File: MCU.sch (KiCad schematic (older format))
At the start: 25 parts, among them J5 ARM_JTAG_SWD_10, U4 STM32F407VGTx

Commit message: Lots of work on routing and pcb layout
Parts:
- C36, C45: footprint Capacitor_SMD:C_0603_1608Metric -> Capacitor_SMD:C_0805_2012Metric
- C50: footprint (none) -> Capacitor_SMD:C_0603_1608Metric
- D1, D2, D7: footprint (none) -> Diode_SMD:D_0603_1608Metric
- J5: footprint (none) -> KTHFS:Atmel_ICP_connector
- R14, R15, R16: footprint (none) -> Resistor_SMD:R_0603_1608Metric
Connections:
- net +3V3: now also U4.19 (VDD)
- net LED_1: now also U4.46 (PE15); no longer U4.35 (PB0)
- net LED_2: now also U4.47 (PB10); no longer U4.36 (PB1)
- net LED_3: now also U4.45 (PE14); no longer U4.37 (PB2)
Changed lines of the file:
@@
 F 0 "C36" H 8565 2546 50  0000 L CNN
 F 1 "1u" H 8565 2455 50  0000 L CNN
-F 2 "Capacitor_SMD:C_0603_1608Metric" H 8488 2350 50  0001 C CNN
+F 2 "Capacitor_SMD:C_0805_2012Metric" H 8488 2350 50  0001 C CNN
 F 3 "~" H 8450 2500 50  0001 C CNN
 	1    8450 2500
@@
 F 0 "J5" H 9150 6200 50  0000 R CNN
 F 1 "ARM_JTAG_SWD_10" H 9450 6100 50  0000 R CNN
-F 2 "" H 9100 5050 50  0001 C CNN
+F 2 "KTHFS:Atmel_ICP_connector" H 9100 5050 50  0001 C CNN
 F 3 "" H 9100 5050 50  0001 C CNN
 	1    9100 5050
@@
 F 0 "D1" H 7493 3795 50  0000 C CNN
 F 1 "LED" H 7493 3886 50  0000 C CNN
-F 2 "" H 7500 4050 50  0001 C CNN
+F 2 "Diode_SMD:D_0603_1608Metric" H 7500 4050 50  0001 C CNN
 F 3 "~" H 7500 4050 50  0001 C CNN
 	1    7500 4050
@@
 F 0 "D2" H 7493 4495 50  0000 C CNN
 F 1 "LED" H 7493 4586 50  0000 C CNN
-F 2 "" H 7500 4750 50  0001 C CNN
+F 2 "Diode_SMD:D_0603_1608Metric" H 7500 4750 50  0001 C CNN
 F 3 "~" H 7500 4750 50  0001 C CNN
 	1    7500 4750
@@
 F 0 "D7" H 7493 5195 50  0000 C CNN
 F 1 "LED" H 7493 5286 50  0000 C CNN
-F 2 "" H 7500 5450 50  0001 C CNN
+F 2 "Diode_SMD:D_0603_1608Metric" H 7500 5450 50  0001 C CNN
 F 3 "~" H 7500 5450 50  0001 C CNN
 	1    7500 5450
@@
 Wire Wire Line
 	4150 4550 4550 4550
-Text Label 5300 3650 2    59   ~ 0
+Text Label 1200 5150 0    59   ~ 0
 LED_1
-Text Label 5300 3750 2    59   ~ 0
+Text Label 5300 4650 2    59   ~ 0
 LED_2
-Text Label 5300 3850 2    59   ~ 0
+Text Label 1200 5050 0    59   ~ 0
 LED_3
 Wire Wire Line
-	4150 3650 5300 3650
-Wire Wire Line
-	4150 3750 5300 3750
-Wire Wire Line
-	4150 3850 5300 3850
+	2350 5150 1200 5150
+Wire Wire Line
+	4150 4650 5300 4650
+Wire Wire Line
+	2350 5050 1200 5050
 Text HLabel 4550 2150 2    59   Output ~ 0
 ~CS_1
@@
 F 0 "C45" H 9515 2521 50  0000 L CNN
 F 1 "1u" H 9515 2430 50  0000 L CNN
-F 2 "Capacitor_SMD:C_0603_1608Metric" H 9438 2325 50  0001 C CNN
+F 2 "Capacitor_SMD:C_0805_2012Metric" H 9438 2325 50  0001 C CNN
 F 3 "~" H 9400 2475 50  0001 C CNN
 	1    9400 2475
@@
 Connection ~ 3250 1450
 Wire Wire Line
-	3250 1450 3050 1450
+	3250 1450 3150 1450
 Connection ~ 3350 1450
 Wire Wire Line
@@
 F 0 "R14" H 1720 1896 50  0000 L CNN
 F 1 "R" H 1720 1805 50  0000 L CNN
-F 2 "" V 1580 1850 50  0001 C CNN
+F 2 "Resistor_SMD:R_0603_1608Metric" V 1580 1850 50  0001 C CNN
 F 3 "~" H 1650 1850 50  0001 C CNN
 	1    1650 1850
@@
 F 0 "R15" H 1720 2496 50  0000 L CNN
 F 1 "R" H 1720 2405 50  0000 L CNN
-F 2 "" V 1580 2450 50  0001 C CNN
+F 2 "Resistor_SMD:R_0603_1608Metric" V 1580 2450 50  0001 C CNN
 F 3 "~" H 1650 2450 50  0001 C CNN
 	1    1650 2450
@@
 F 0 "R16" H 10570 4496 50  0000 L CNN
 F 1 "10k" H 10570 4405 50  0000 L CNN
-F 2 "" V 10430 4450 50  0001 C CNN
+F 2 "Resistor_SMD:R_0603_1608Metric" V 10430 4450 50  0001 C CNN
 F 3 "~" H 10500 4450 50  0001 C CNN
 	1    10500 4450
@@
 F 0 "C50" H 10615 4996 50  0000 L CNN
 F 1 "C" H 10615 4905 50  0000 L CNN
-F 2 "" H 10538 4800 50  0001 C CNN
+F 2 "Capacitor_SMD:C_0603_1608Metric" H 10538 4800 50  0001 C CNN
 F 3 "~" H 10500 4950 50  0001 C CNN
 	1    10500 4950
@@
 Wire Notes Line
 	11050 700  7750 700
+Wire Wire Line
+	3150 1450 3150 1650
+Connection ~ 3150 1450
+Wire Wire Line
+	3150 1450 3050 1450
 $EndSCHEMATC

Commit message: More routing changes
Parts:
- added R19, R20: 0, Resistor_SMD:R_0603_1608Metric, symbol Device:R
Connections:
- net HGM: now also U4.3 (PE4); no longer U4.90 (PB4)
- net LNA_EN: now also U4.4 (PE5); no longer U4.91 (PB5)
- net MISO: now also U4.79 (PC11); no longer U4.31 (PA6)
- net MOSI: now also U4.80 (PC12); no longer U4.32 (PA7)
- net PA_EN: now also U4.5 (PE6); no longer U4.92 (PB6)
- net RF_GPIO0: now also U4.89 (PB3); no longer U4.96 (PB9)
- net RF_GPIO2: now also U4.90 (PB4); no longer U4.95 (PB8)
- net RF_GPIO3: now also U4.91 (PB5); no longer U4.93 (PB7)
- net SLCK: now also U4.78 (PC10); no longer U4.30 (PA5)
- net ~CS_1: now also R20.1; no longer U4.25 (PA2)
- net RF2_DIO5: now reaches U4.33 (PC4)
- net RF2_DIO3: now reaches U4.34 (PC5)
- net RF2_DIO4: now reaches U4.35 (PB0)
- net RF2_DIO0: now reaches U4.36 (PB1)
- net RF2_DIO1: now reaches U4.37 (PB2)
- net RF2_DIO2: now reaches U4.38 (PE7)
- net at U4.87 (PD6): now also R20.2
- new net: R19.2, U4.93 (PB7)
- new net MISO_RF2: U4.31 (PA6)
- new net MOSI_RF2: U4.32 (PA7)
- new net SLCK_RF2: U4.30 (PA5)
- new net ~RESET: R19.1
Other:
- note added: "SPI3"
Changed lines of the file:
@@
 $EndDescr
 Text HLabel 4550 2450 2    59   Output ~ 0
-SLCK
+SLCK_RF2
 Text HLabel 4550 2650 2    59   Output ~ 0
-MOSI
-Text HLabel 4550 2250 2    59   Output ~ 0
-~CS_2
+MOSI_RF2
 Text HLabel 4550 3150 2    50   Input ~ 0
 CAN_TX_1
@@
 Wire Notes Line
 	8050 6150 8050 3550
-Text HLabel 4550 4050 2    59   Output ~ 0
+Text HLabel 1950 4050 0    59   Output ~ 0
 HGM
-Text HLabel 4550 4150 2    59   Output ~ 0
+Text HLabel 1950 4150 0    59   Output ~ 0
 LNA_EN
-Text HLabel 4550 4250 2    59   Output ~ 0
+Text HLabel 1950 4250 0    59   Output ~ 0
 PA_EN
-Text HLabel 4550 4550 2    59   BiDi ~ 0
-RF_GPIO0
-Text HLabel 4550 4450 2    59   BiDi ~ 0
-RF_GPIO2
-Text HLabel 4550 4350 2    59   BiDi ~ 0
+Text HLabel 4550 4150 2    59   BiDi ~ 0
 RF_GPIO3
-Wire Wire Line
-	4550 2250 4150 2250
 Wire Wire Line
 	4150 2450 4550 2450
@@
 Text Notes 5050 5000 0    59   ~ 0
 CAN3\n\n
-Text Notes 4875 2575 0    59   ~ 0
+Text Notes 5200 2600 0    59   ~ 0
 SPI1
 Wire Wire Line
-	4150 4050 4550 4050
+	2350 4250 1950 4250
+Wire Wire Line
+	2350 4150 1950 4150
+Wire Wire Line
+	2350 4050 1950 4050
 Wire Wire Line
 	4150 4150 4550 4150
-Wire Wire Line
-	4150 4250 4550 4250
-Wire Wire Line
-	4150 4350 4550 4350
-Wire Wire Line
-	4150 4450 4550 4450
-Wire Wire Line
-	4150 4550 4550 4550
 Text Label 1200 5150 0    59   ~ 0
 LED_1
@@
 Wire Wire Line
 	2350 5050 1200 5050
-Text HLabel 4550 2150 2    59   Output ~ 0
+Text HLabel 1950 5950 0    59   Output ~ 0
 ~CS_1
-Wire Wire Line
-	4550 2150 4150 2150
 Text Notes 9100 1975 0    59   ~ 0
 VREF\n
@@
 	4150 2550 4550 2550
 Text HLabel 4550 2550 2    59   Input ~ 0
-MISO
+MISO_RF2
 Text Label 5300 3350 2    59   ~ 0
 SWCLK
@@
 Wire Wire Line
 	3150 1450 3050 1450
+Text HLabel 4550 3750 2    59   BiDi ~ 0
+RF2_DIO0
+Text HLabel 4550 3850 2    59   BiDi ~ 0
+RF2_DIO1
+Text HLabel 1950 4350 0    59   BiDi ~ 0
+RF2_DIO2
+Text HLabel 4550 5850 2    59   BiDi ~ 0
+RF2_DIO3
+Text HLabel 4550 3650 2    59   BiDi ~ 0
+RF2_DIO4
+Text HLabel 4550 5750 2    59   BiDi ~ 0
+RF2_DIO5
+Wire Wire Line
+	4550 2250 4150 2250
+Text HLabel 4550 2250 2    59   Output ~ 0
+~CS_2
+Wire Wire Line
+	5100 3450 5500 3450
+Text HLabel 5500 3450 2    59   Output ~ 0
+RESET_RF2
+Text HLabel 4550 4350 2    50   Output ~ 0
+~RESET
+$Comp
+L Device:R R19
+U 1 1 6039C6F6
+P 4300 4350
+F 0 "R19" V 4200 4300 50  0000 C CNN
+F 1 "0" V 4200 4425 50  0000 C CNN
+F 2 "Resistor_SMD:R_0603_1608Metric" V 4230 4350 50  0001 C CNN
+F 3 "~" H 4300 4350 50  0001 C CNN
+	1    4300 4350
+	0    1    1    0
+$EndComp
+Wire Wire Line
+	4450 4350 4550 4350
+Wire Wire Line
+	4550 3750 4150 3750
+Wire Wire Line
+	4550 3850 4150 3850
+Wire Wire Line
+	1950 4350 2350 4350
+Wire Wire Line
+	4550 3650 4150 3650
+Wire Wire Line
+	4550 5750 4150 5750
+Wire Wire Line
+	4550 5850 4150 5850
+$Comp
+L Device:R R20
+U 1 1 603E4876
+P 2200 5950
+F 0 "R20" V 2100 5900 50  0000 C CNN
+F 1 "0" V 2100 6025 50  0000 C CNN
+F 2 "Resistor_SMD:R_0603_1608Metric" V 2130 5950 50  0001 C CNN
+F 3 "~" H 2200 5950 50  0001 C CNN
+	1    2200 5950
+	0    -1   -1   0
+$EndComp
+Wire Wire Line
+	2050 5950 1950 5950
+Text HLabel 4550 6350 2    59   Output ~ 0
+SLCK
+Text HLabel 4550 6550 2    59   Output ~ 0
+MOSI
+Text HLabel 4550 6450 2    59   Input ~ 0
+MISO
+Wire Wire Line
+	4150 6350 4550 6350
+Wire Wire Line
+	4550 6450 4150 6450
+Text Notes 4900 6500 0    59   ~ 0
+SPI3
+Wire Wire Line
+	4550 6550 4150 6550
+Wire Wire Line
+	4150 4050 4550 4050
+Text HLabel 4550 4050 2    59   BiDi ~ 0
+RF_GPIO2
+Wire Wire Line
+	4150 3950 4550 3950
+Text HLabel 4550 3950 2    59   BiDi ~ 0
+RF_GPIO0
 $EndSCHEMATC

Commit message: Added edge cuts and silk screen comments
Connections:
- net RESET_RF2: now also U4.8 (PC14)
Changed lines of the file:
@@
 ~CS_2
 Wire Wire Line
-	5100 3450 5500 3450
-Text HLabel 5500 3450 2    59   Output ~ 0
+	4150 6750 4550 6750
+Text HLabel 4550 6750 2    59   Output ~ 0
 RESET_RF2
 Text HLabel 4550 4350 2    50   Output ~ 0

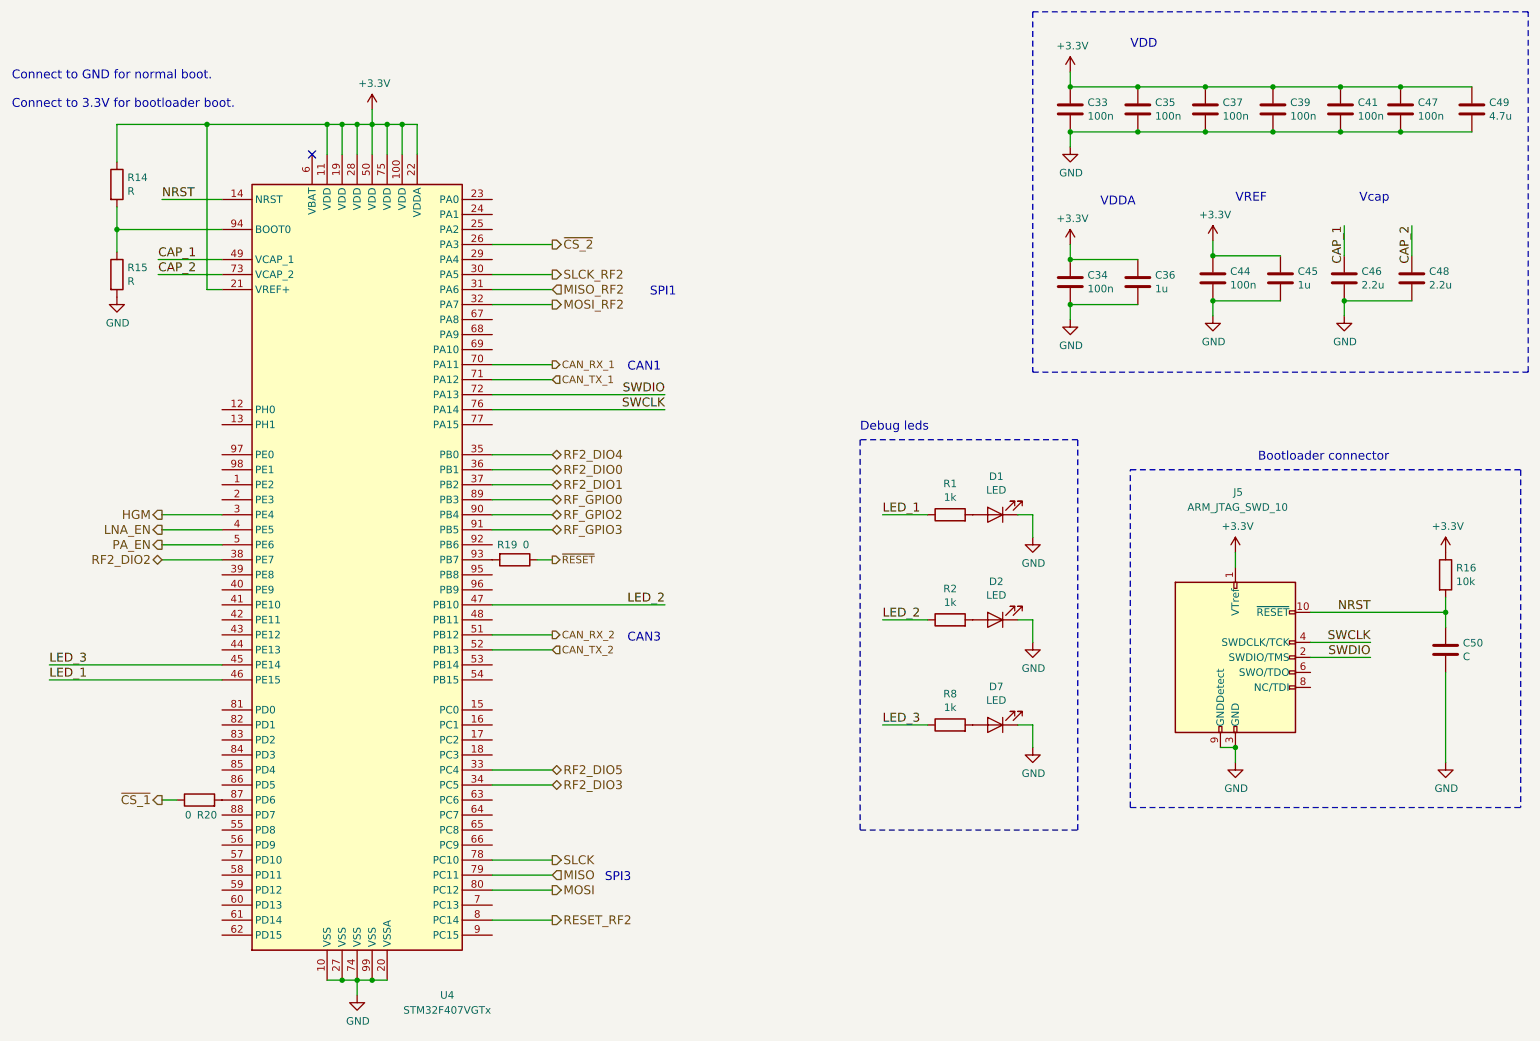
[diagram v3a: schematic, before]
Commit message: Added mounting holes and terminal block
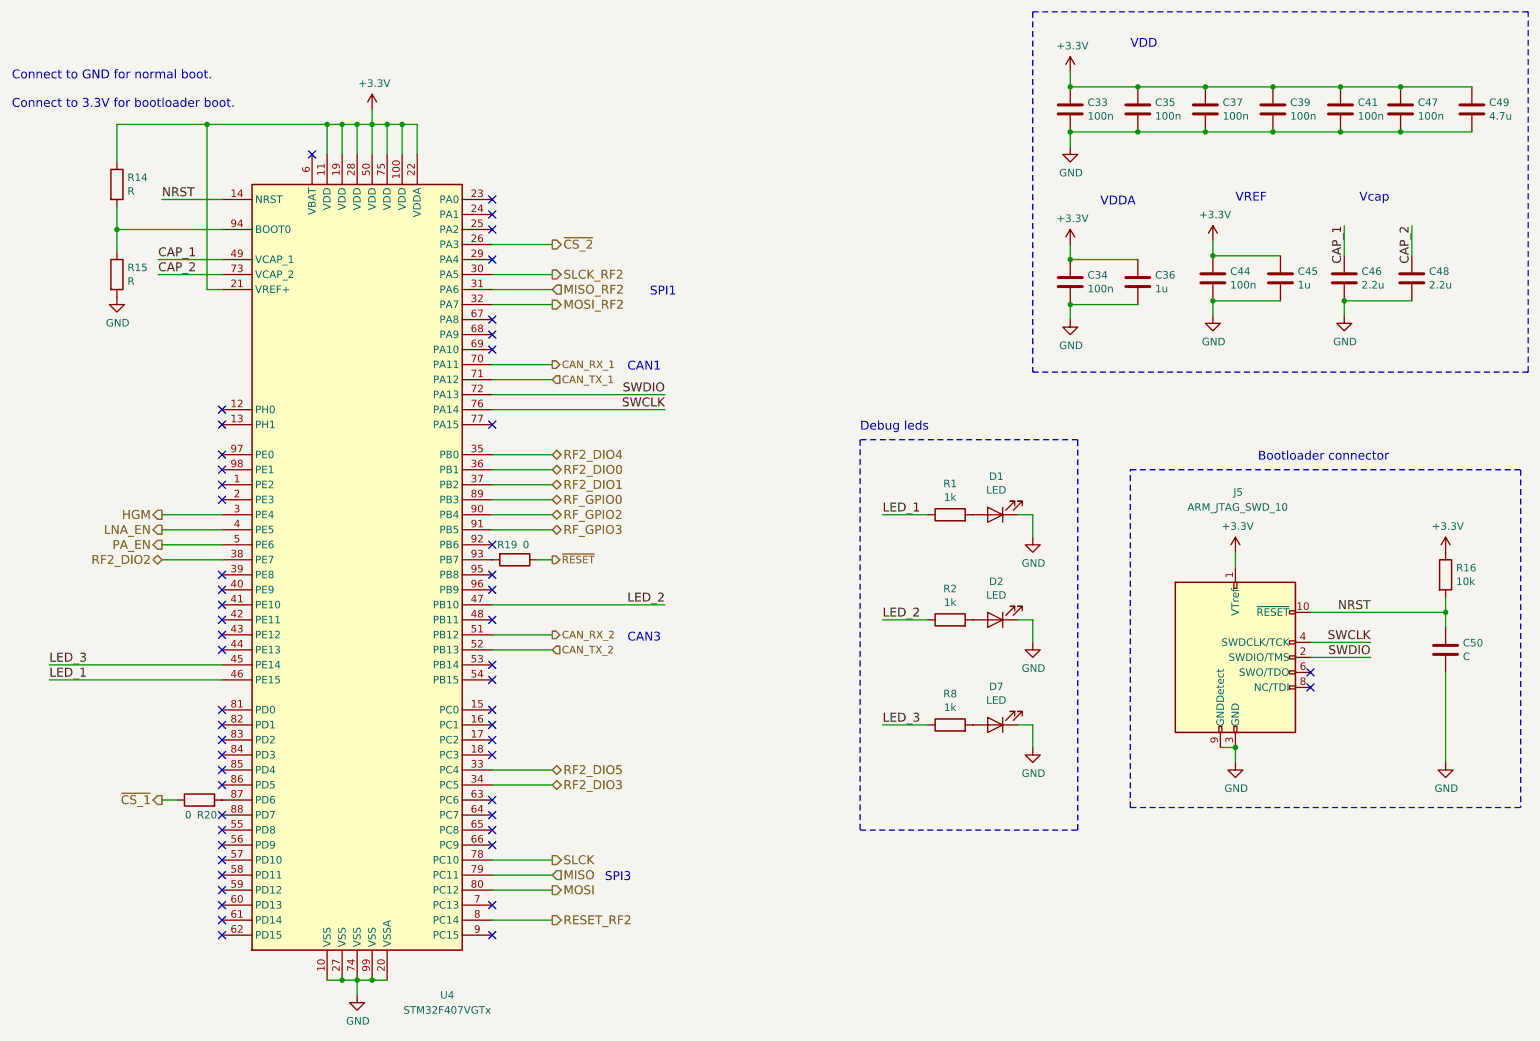
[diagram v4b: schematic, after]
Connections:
- no-connect marks 1 -> 54
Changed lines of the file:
@@
 Text HLabel 4550 3950 2    59   BiDi ~ 0
 RF_GPIO0
+NoConn ~ 4150 1950
+NoConn ~ 4150 2050
+NoConn ~ 4150 2150
+NoConn ~ 4150 2350
+NoConn ~ 4150 2750
+NoConn ~ 4150 2850
+NoConn ~ 4150 2950
+NoConn ~ 4150 3450
+NoConn ~ 4150 4450
+NoConn ~ 4150 4550
+NoConn ~ 4150 4250
+NoConn ~ 4150 4750
+NoConn ~ 4150 5050
+NoConn ~ 4150 5150
+NoConn ~ 4150 5350
+NoConn ~ 4150 5450
+NoConn ~ 4150 5550
+NoConn ~ 4150 5650
+NoConn ~ 4150 5950
+NoConn ~ 4150 6050
+NoConn ~ 4150 6150
+NoConn ~ 4150 6250
+NoConn ~ 4150 6650
+NoConn ~ 4150 6850
+NoConn ~ 2350 6050
+NoConn ~ 2350 6150
+NoConn ~ 2350 6250
+NoConn ~ 2350 6350
+NoConn ~ 2350 6450
+NoConn ~ 2350 6550
+NoConn ~ 2350 6650
+NoConn ~ 2350 6750
+NoConn ~ 2350 6850
+NoConn ~ 2350 5350
+NoConn ~ 2350 5450
+NoConn ~ 2350 5550
+NoConn ~ 2350 5650
+NoConn ~ 2350 5750
+NoConn ~ 2350 5850
+NoConn ~ 2350 4450
+NoConn ~ 2350 4550
+NoConn ~ 2350 4650
+NoConn ~ 2350 4750
+NoConn ~ 2350 4850
+NoConn ~ 2350 4950
+NoConn ~ 2350 3350
+NoConn ~ 2350 3450
+NoConn ~ 2350 3650
+NoConn ~ 2350 3750
+NoConn ~ 2350 3850
+NoConn ~ 2350 3950
+NoConn ~ 9600 5100
+NoConn ~ 9600 5200
 $EndSCHEMATC

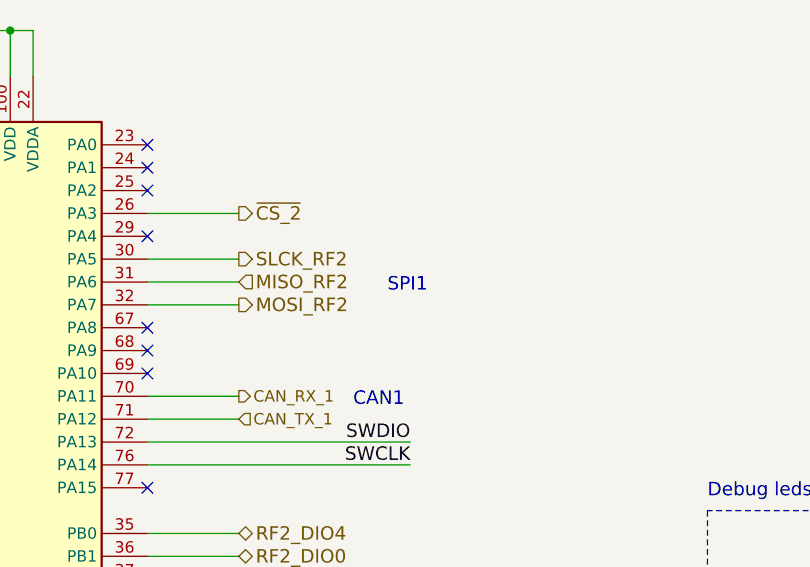
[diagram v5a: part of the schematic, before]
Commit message: Added guard ring and cleaned up silkscreen
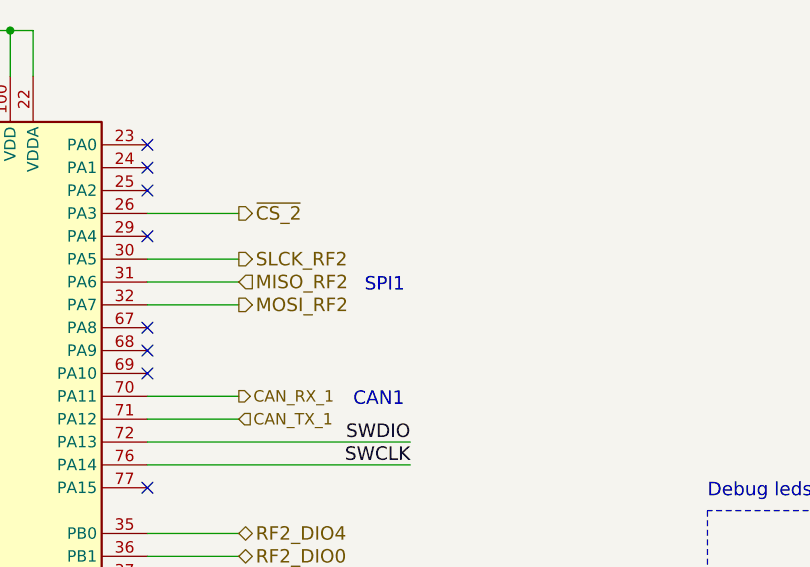
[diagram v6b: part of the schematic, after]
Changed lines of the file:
@@
 Text Notes 5050 5000 0    59   ~ 0
 CAN3\n\n
-Text Notes 5200 2600 0    59   ~ 0
+Text Notes 5100 2600 0    59   ~ 0
 SPI1
 Wire Wire Line

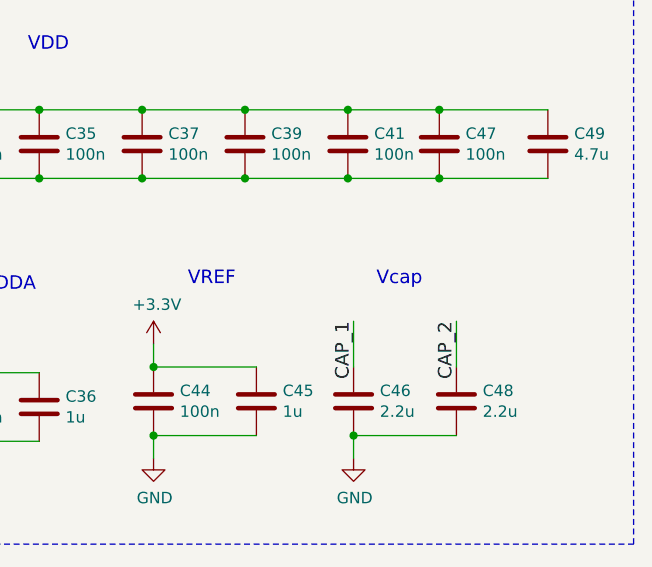
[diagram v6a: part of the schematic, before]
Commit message: Fixed (most) pwr flag issues
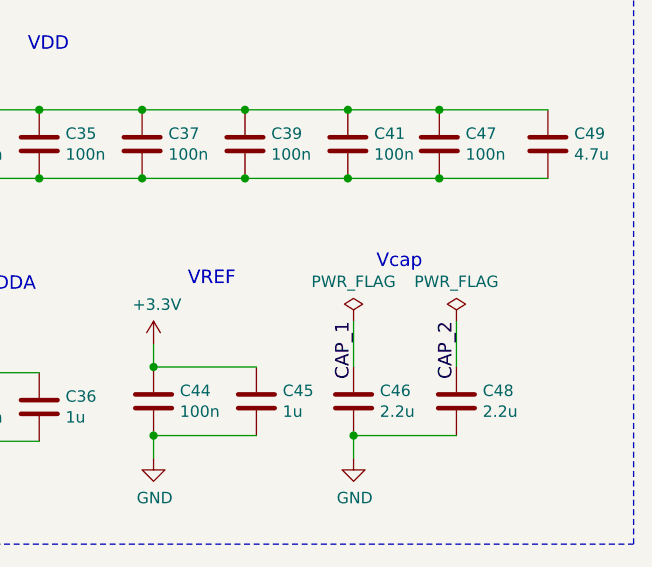
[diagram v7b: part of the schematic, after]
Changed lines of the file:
@@
 Text Label 10275 2125 3    59   ~ 0
 CAP_2
-Text Notes 9925 1975 0    59   ~ 0
+Text Notes 9925 1900 0    59   ~ 0
 Vcap\n
 NoConn ~ 2950 1650
@@
 NoConn ~ 9600 5100
 NoConn ~ 9600 5200
+$Comp
+L power:PWR_FLAG #FLG?
+U 1 1 60322F2C
+P 9825 2125
+F 0 "#FLG?" H 9825 2200 50  0001 C CNN
+F 1 "PWR_FLAG" H 9825 2298 50  0000 C CNN
+F 2 "" H 9825 2125 50  0001 C CNN
+F 3 "~" H 9825 2125 50  0001 C CNN
+	1    9825 2125
+	1    0    0    -1
+$EndComp
+$Comp
+L power:PWR_FLAG #FLG?
+U 1 1 60324024
+P 10275 2125
+F 0 "#FLG?" H 10275 2200 50  0001 C CNN
+F 1 "PWR_FLAG" H 10275 2298 50  0000 C CNN
+F 2 "" H 10275 2125 50  0001 C CNN
+F 3 "~" H 10275 2125 50  0001 C CNN
+	1    10275 2125
+	1    0    0    -1
+$EndComp
 $EndSCHEMATC
